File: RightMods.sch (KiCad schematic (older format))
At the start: 9 parts

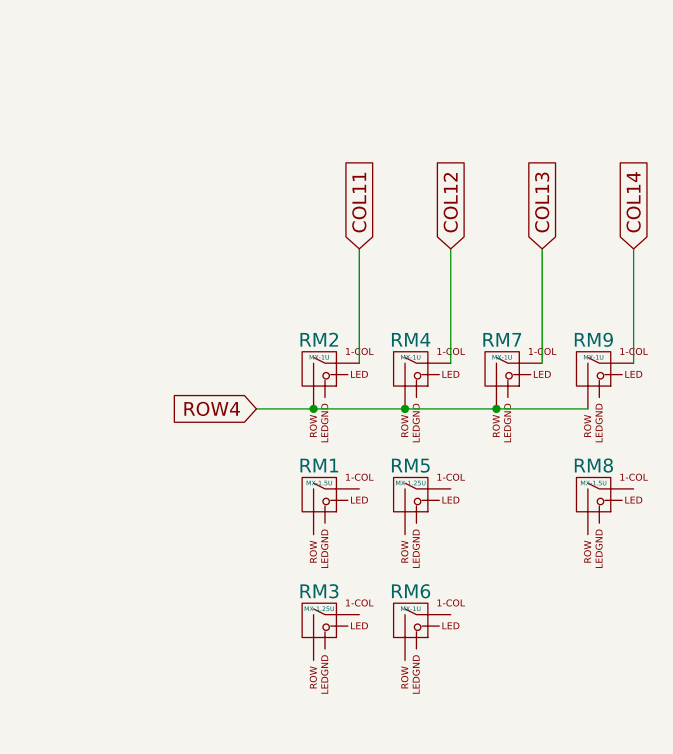
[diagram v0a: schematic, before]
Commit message: Add LEDs
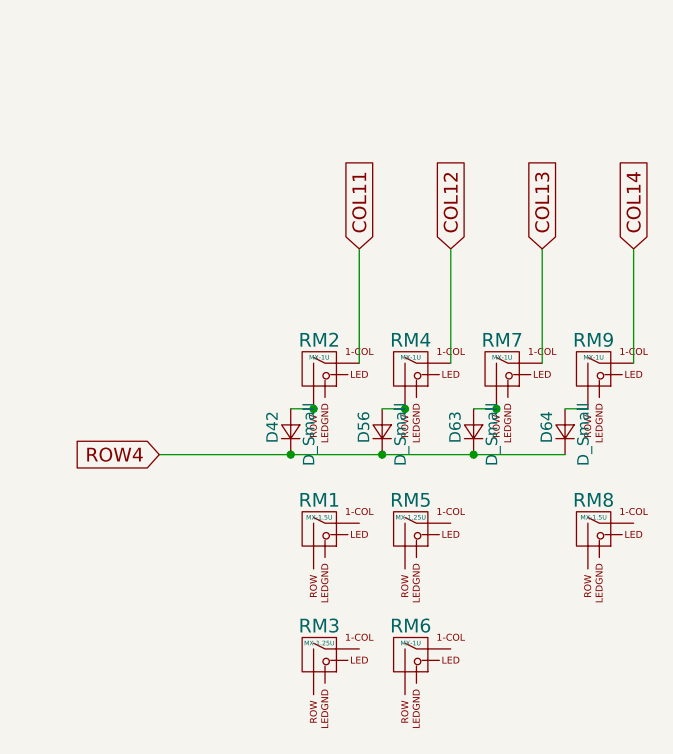
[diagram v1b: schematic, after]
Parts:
- added D42, D56, D63, D64: D_Small, symbol D_Small
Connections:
- net ROW4: now also D42.1 (K), D56.1 (K), D63.1 (K), D64.1 (K); no longer RM2.2 (ROW), RM4.2 (ROW), RM7.2 (ROW), RM9.2 (ROW)
- new net: D42.2 (A), RM2.2 (ROW)
- new net: D56.2 (A), RM4.2 (ROW)
- new net: D63.2 (A), RM7.2 (ROW)
- new net: D64.2 (A), RM9.2 (ROW)
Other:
- moved on the sheet: RM1, RM3, RM5, RM6, RM8
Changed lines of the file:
@@
 L MX-1U RM1
 U 1 1 5A785255
-P 2450 2850
-F 0 "RM1" H 2450 2975 60  0000 C CNN
-F 1 "MX-1.5U" H 2450 2900 20  0000 C CNN
-F 2 "MX_Alps_Hybrid:MX-1.5U-NoLED" H 2425 2825 60  0001 C CNN
-F 3 "" H 2425 2825 60  0001 C CNN
-	1    2450 2850
+P 2450 3000
+F 0 "RM1" H 2450 3125 60  0000 C CNN
+F 1 "MX-1.5U" H 2450 3050 20  0000 C CNN
+F 2 "MX_Alps_Hybrid:MX-1.5U-NoLED" H 2425 2975 60  0001 C CNN
+F 3 "" H 2425 2975 60  0001 C CNN
+	1    2450 3000
 	1    0    0    -1
 $EndComp
@@
 L MX-1U RM3
 U 1 1 5A785291
-P 2450 3400
-F 0 "RM3" H 2450 3525 60  0000 C CNN
-F 1 "MX-1.25U" H 2450 3450 20  0000 C CNN
-F 2 "MX_Alps_Hybrid:MX-1.25U-NoLED" H 2425 3375 60  0001 C CNN
-F 3 "" H 2425 3375 60  0001 C CNN
-	1    2450 3400
+P 2450 3550
+F 0 "RM3" H 2450 3675 60  0000 C CNN
+F 1 "MX-1.25U" H 2450 3600 20  0000 C CNN
+F 2 "MX_Alps_Hybrid:MX-1.25U-NoLED" H 2425 3525 60  0001 C CNN
+F 3 "" H 2425 3525 60  0001 C CNN
+	1    2450 3550
 	1    0    0    -1
 $EndComp
@@
 L MX-1U RM5
 U 1 1 5A785372
-P 2850 2850
-F 0 "RM5" H 2850 2975 60  0000 C CNN
-F 1 "MX-1.25U" H 2850 2900 20  0000 C CNN
-F 2 "MX_Alps_Hybrid:MX-1.25U-NoLED" H 2825 2825 60  0001 C CNN
-F 3 "" H 2825 2825 60  0001 C CNN
-	1    2850 2850
+P 2850 3000
+F 0 "RM5" H 2850 3125 60  0000 C CNN
+F 1 "MX-1.25U" H 2850 3050 20  0000 C CNN
+F 2 "MX_Alps_Hybrid:MX-1.25U-NoLED" H 2825 2975 60  0001 C CNN
+F 3 "" H 2825 2975 60  0001 C CNN
+	1    2850 3000
 	1    0    0    -1
 $EndComp
@@
 L MX-1U RM6
 U 1 1 5A7856EF
-P 2850 3400
-F 0 "RM6" H 2850 3525 60  0000 C CNN
-F 1 "MX-1U" H 2850 3450 20  0000 C CNN
-F 2 "MX_Alps_Hybrid:MX-1U-NoLED" H 2825 3375 60  0001 C CNN
-F 3 "" H 2825 3375 60  0001 C CNN
-	1    2850 3400
+P 2850 3550
+F 0 "RM6" H 2850 3675 60  0000 C CNN
+F 1 "MX-1U" H 2850 3600 20  0000 C CNN
+F 2 "MX_Alps_Hybrid:MX-1U-NoLED" H 2825 3525 60  0001 C CNN
+F 3 "" H 2825 3525 60  0001 C CNN
+	1    2850 3550
 	1    0    0    -1
 $EndComp
@@
 L MX-1U RM8
 U 1 1 5A7858EC
-P 3650 2850
-F 0 "RM8" H 3650 2975 60  0000 C CNN
-F 1 "MX-1.5U" H 3650 2900 20  0000 C CNN
-F 2 "MX_Alps_Hybrid:MX-1.5U-NoLED" H 3625 2825 60  0001 C CNN
-F 3 "" H 3625 2825 60  0001 C CNN
-	1    3650 2850
+P 3650 3000
+F 0 "RM8" H 3650 3125 60  0000 C CNN
+F 1 "MX-1.5U" H 3650 3050 20  0000 C CNN
+F 2 "MX_Alps_Hybrid:MX-1.5U-NoLED" H 3625 2975 60  0001 C CNN
+F 3 "" H 3625 2975 60  0001 C CNN
+	1    3650 3000
 	1    0    0    -1
 $EndComp
@@
 Text GLabel 3825 1775 1    60   Input ~ 0
 COL14
-Wire Wire Line
-	2175 2475 3625 2475
 Connection ~ 3225 2475
 Connection ~ 2825 2475
 Connection ~ 2425 2475
-Text GLabel 2175 2475 0    60   Input ~ 0
+Text GLabel 1750 2675 0    60   Input ~ 0
 ROW4
+$Comp
+L D_Small D42
+U 1 1 5A789BFF
+P 2325 2575
+F 0 "D42" H 2275 2655 50  0000 L CNN
+F 1 "D_Small" H 2175 2495 50  0000 L CNN
+F 2 "" V 2325 2575 50  0001 C CNN
+F 3 "" V 2325 2575 50  0001 C CNN
+	1    2325 2575
+	0    -1   -1   0
+$EndComp
+$Comp
+L D_Small D56
+U 1 1 5A789E12
+P 2725 2575
+F 0 "D56" H 2675 2655 50  0000 L CNN
+F 1 "D_Small" H 2575 2495 50  0000 L CNN
+F 2 "" V 2725 2575 50  0001 C CNN
+F 3 "" V 2725 2575 50  0001 C CNN
+	1    2725 2575
+	0    -1   -1   0
+$EndComp
+$Comp
+L D_Small D63
+U 1 1 5A789F57
+P 3125 2575
+F 0 "D63" H 3075 2655 50  0000 L CNN
+F 1 "D_Small" H 2975 2495 50  0000 L CNN
+F 2 "" V 3125 2575 50  0001 C CNN
+F 3 "" V 3125 2575 50  0001 C CNN
+	1    3125 2575
+	0    -1   -1   0
+$EndComp
+$Comp
+L D_Small D64
+U 1 1 5A78A02B
+P 3525 2575
+F 0 "D64" H 3475 2655 50  0000 L CNN
+F 1 "D_Small" H 3375 2495 50  0000 L CNN
+F 2 "" V 3525 2575 50  0001 C CNN
+F 3 "" V 3525 2575 50  0001 C CNN
+	1    3525 2575
+	0    -1   -1   0
+$EndComp
+Wire Wire Line
+	3625 2475 3525 2475
+Wire Wire Line
+	3225 2475 3125 2475
+Wire Wire Line
+	2825 2475 2725 2475
+Wire Wire Line
+	2325 2475 2425 2475
+Wire Wire Line
+	1750 2675 3525 2675
+Connection ~ 3125 2675
+Connection ~ 2725 2675
+Connection ~ 2325 2675
 $EndSCHEMATC

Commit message: Place LEDs and move out diodes
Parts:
- D42, D56, D63, D64: footprint (none) -> Diodes_SMD:D_SOD-123
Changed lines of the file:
@@
 F 0 "D42" H 2275 2655 50  0000 L CNN
 F 1 "D_Small" H 2175 2495 50  0000 L CNN
-F 2 "" V 2325 2575 50  0001 C CNN
+F 2 "Diodes_SMD:D_SOD-123" V 2325 2575 50  0001 C CNN
 F 3 "" V 2325 2575 50  0001 C CNN
 	1    2325 2575
@@
 F 0 "D56" H 2675 2655 50  0000 L CNN
 F 1 "D_Small" H 2575 2495 50  0000 L CNN
-F 2 "" V 2725 2575 50  0001 C CNN
+F 2 "Diodes_SMD:D_SOD-123" V 2725 2575 50  0001 C CNN
 F 3 "" V 2725 2575 50  0001 C CNN
 	1    2725 2575
@@
 F 0 "D63" H 3075 2655 50  0000 L CNN
 F 1 "D_Small" H 2975 2495 50  0000 L CNN
-F 2 "" V 3125 2575 50  0001 C CNN
+F 2 "Diodes_SMD:D_SOD-123" V 3125 2575 50  0001 C CNN
 F 3 "" V 3125 2575 50  0001 C CNN
 	1    3125 2575
@@
 F 0 "D64" H 3475 2655 50  0000 L CNN
 F 1 "D_Small" H 3375 2495 50  0000 L CNN
-F 2 "" V 3525 2575 50  0001 C CNN
+F 2 "Diodes_SMD:D_SOD-123" V 3525 2575 50  0001 C CNN
 F 3 "" V 3525 2575 50  0001 C CNN
 	1    3525 2575

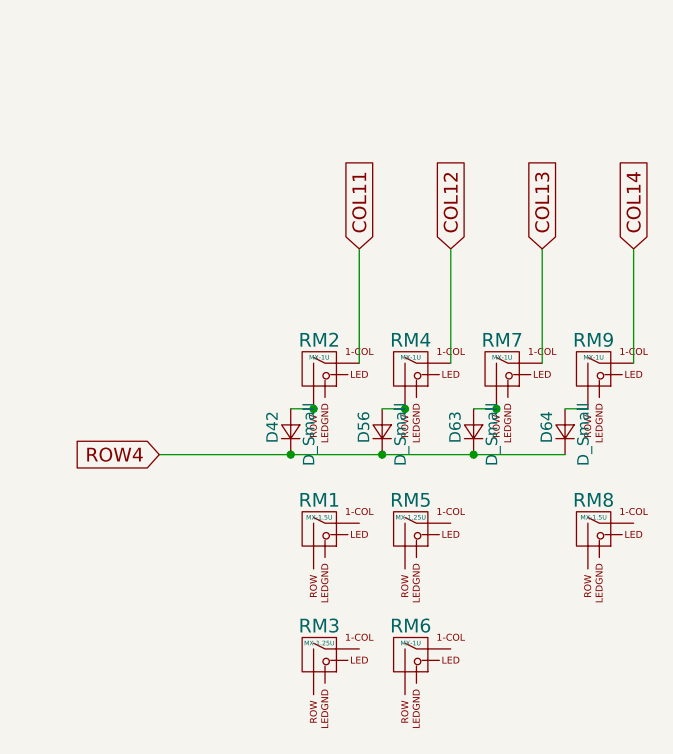
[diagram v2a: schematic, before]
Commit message: Route RM1, right mod leds
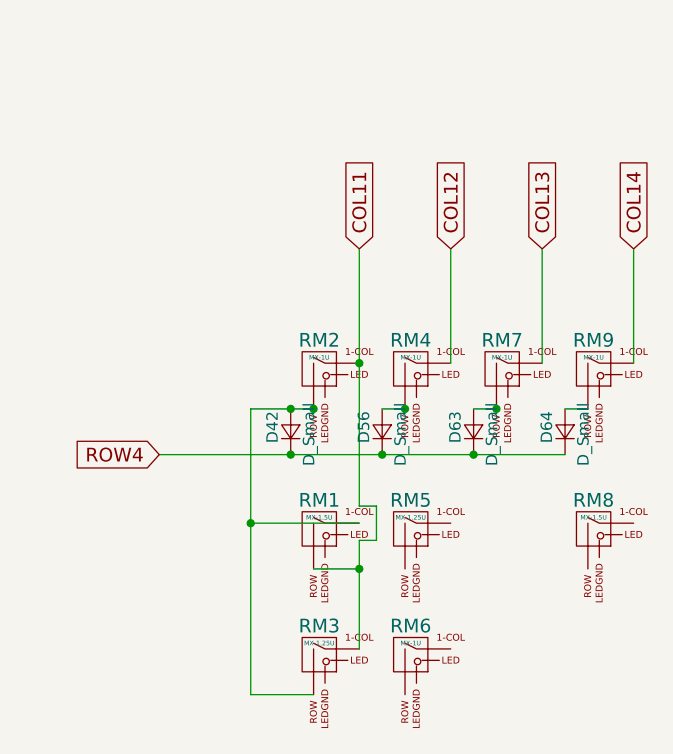
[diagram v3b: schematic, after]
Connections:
- net COL11: now also RM1.2 (ROW), RM3.1 (COL)
- net at D42.2 (A), RM2.2 (ROW): now also RM1.1 (COL), RM3.2 (ROW)
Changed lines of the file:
@@
 $EndComp
 Wire Wire Line
-	2625 2275 2625 1775
+	2625 1775 2625 2900
 Text GLabel 2625 1775 1    60   Input ~ 0
 COL11
@@
 	2825 2475 2725 2475
 Wire Wire Line
-	2325 2475 2425 2475
+	2150 2475 2425 2475
 Wire Wire Line
 	1750 2675 3525 2675
@@
 Connection ~ 2725 2675
 Connection ~ 2325 2675
+Wire Wire Line
+	2625 2900 2700 2900
+Wire Wire Line
+	2700 2900 2700 3050
+Wire Wire Line
+	2700 3050 2625 3050
+Wire Wire Line
+	2625 3050 2625 3525
+Connection ~ 2625 2275
+Wire Wire Line
+	2150 2475 2150 3725
+Wire Wire Line
+	2150 3725 2425 3725
+Connection ~ 2325 2475
+Wire Wire Line
+	2625 2975 2150 2975
+Connection ~ 2150 2975
+Wire Wire Line
+	2425 3175 2625 3175
+Connection ~ 2625 3175
 $EndSCHEMATC

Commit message: Finish routing
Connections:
- net COL12: now also RM5.2 (ROW), RM6.2 (ROW)
- net COL14: now also RM8.1 (COL), RM9.2 (ROW); no longer RM9.1 (COL)
- net at D56.2 (A), RM4.2 (ROW): now also RM5.1 (COL), RM6.1 (COL)
- net at D64.2 (A): now also RM8.2 (ROW), RM9.1 (COL); no longer RM9.2 (ROW)
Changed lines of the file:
@@
 	1    0    0    -1
 $EndComp
-Wire Wire Line
-	2625 1775 2625 2900
 Text GLabel 2625 1775 1    60   Input ~ 0
 COL11
-Wire Wire Line
-	3025 2275 3025 1775
 Text GLabel 3025 1775 1    60   Input ~ 0
 COL12
-Wire Wire Line
-	3425 2275 3425 1775
 Text GLabel 3425 1775 1    60   Input ~ 0
 COL13
-Wire Wire Line
-	3825 2275 3825 1775
 Text GLabel 3825 1775 1    60   Input ~ 0
 COL14
-Connection ~ 3225 2475
-Connection ~ 2825 2475
-Connection ~ 2425 2475
 Text GLabel 1750 2675 0    60   Input ~ 0
 ROW4
@@
 $EndComp
 Wire Wire Line
-	3625 2475 3525 2475
+	2625 1775 2625 2900
+Wire Wire Line
+	3025 1775 3025 2800
+Wire Wire Line
+	3425 2275 3425 1775
+Connection ~ 3225 2475
+Connection ~ 2825 2475
+Connection ~ 2425 2475
 Wire Wire Line
 	3225 2475 3125 2475
 Wire Wire Line
-	2825 2475 2725 2475
+	2725 2475 3075 2475
 Wire Wire Line
 	2150 2475 2425 2475
@@
 	2425 3175 2625 3175
 Connection ~ 2625 3175
+Wire Wire Line
+	3025 2800 2750 2800
+Wire Wire Line
+	2750 2800 2750 3725
+Wire Wire Line
+	2750 3175 2825 3175
+Connection ~ 3025 2275
+Wire Wire Line
+	2750 3725 2825 3725
+Connection ~ 2750 3175
+Wire Wire Line
+	3075 2475 3075 3525
+Wire Wire Line
+	3075 2975 3025 2975
+Wire Wire Line
+	3075 3525 3025 3525
+Connection ~ 3075 2975
+Wire Wire Line
+	3525 2475 3525 2275
+Wire Wire Line
+	3525 2275 3825 2275
+Wire Wire Line
+	3825 1775 3825 2200
+Wire Wire Line
+	3825 2200 3900 2200
+Wire Wire Line
+	3900 2200 3900 2975
+Wire Wire Line
+	3900 2475 3625 2475
+Wire Wire Line
+	3900 2975 3825 2975
+Connection ~ 3900 2475
+Wire Wire Line
+	3525 2475 3575 2475
+Wire Wire Line
+	3575 2475 3575 3175
+Wire Wire Line
+	3575 3175 3625 3175
 $EndSCHEMATC

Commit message: Revert LED structure
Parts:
- RM1, RM8: footprint MX_Alps_Hybrid:MX-1.5U-NoLED -> MX_Alps_Hybrid:MX-1.5U
- RM2, RM4, RM6, RM7, RM9: footprint MX_Alps_Hybrid:MX-1U-NoLED -> MX_Alps_Hybrid:MX-1U
- RM3, RM5: footprint MX_Alps_Hybrid:MX-1.25U-NoLED -> MX_Alps_Hybrid:MX-1.25U
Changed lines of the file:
@@
 F 0 "RM2" H 2450 2425 60  0000 C CNN
 F 1 "MX-1U" H 2450 2350 20  0000 C CNN
-F 2 "MX_Alps_Hybrid:MX-1U-NoLED" H 2425 2275 60  0001 C CNN
+F 2 "MX_Alps_Hybrid:MX-1U" H 2425 2275 60  0001 C CNN
 F 3 "" H 2425 2275 60  0001 C CNN
 	1    2450 2300
@@
 F 0 "RM1" H 2450 3125 60  0000 C CNN
 F 1 "MX-1.5U" H 2450 3050 20  0000 C CNN
-F 2 "MX_Alps_Hybrid:MX-1.5U-NoLED" H 2425 2975 60  0001 C CNN
+F 2 "MX_Alps_Hybrid:MX-1.5U" H 2425 2975 60  0001 C CNN
 F 3 "" H 2425 2975 60  0001 C CNN
 	1    2450 3000
@@
 F 0 "RM3" H 2450 3675 60  0000 C CNN
 F 1 "MX-1.25U" H 2450 3600 20  0000 C CNN
-F 2 "MX_Alps_Hybrid:MX-1.25U-NoLED" H 2425 3525 60  0001 C CNN
+F 2 "MX_Alps_Hybrid:MX-1.25U" H 2425 3525 60  0001 C CNN
 F 3 "" H 2425 3525 60  0001 C CNN
 	1    2450 3550
@@
 F 0 "RM4" H 2850 2425 60  0000 C CNN
 F 1 "MX-1U" H 2850 2350 20  0000 C CNN
-F 2 "MX_Alps_Hybrid:MX-1U-NoLED" H 2825 2275 60  0001 C CNN
+F 2 "MX_Alps_Hybrid:MX-1U" H 2825 2275 60  0001 C CNN
 F 3 "" H 2825 2275 60  0001 C CNN
 	1    2850 2300
@@
 F 0 "RM5" H 2850 3125 60  0000 C CNN
 F 1 "MX-1.25U" H 2850 3050 20  0000 C CNN
-F 2 "MX_Alps_Hybrid:MX-1.25U-NoLED" H 2825 2975 60  0001 C CNN
+F 2 "MX_Alps_Hybrid:MX-1.25U" H 2825 2975 60  0001 C CNN
 F 3 "" H 2825 2975 60  0001 C CNN
 	1    2850 3000
@@
 F 0 "RM7" H 3250 2425 60  0000 C CNN
 F 1 "MX-1U" H 3250 2350 20  0000 C CNN
-F 2 "MX_Alps_Hybrid:MX-1U-NoLED" H 3225 2275 60  0001 C CNN
+F 2 "MX_Alps_Hybrid:MX-1U" H 3225 2275 60  0001 C CNN
 F 3 "" H 3225 2275 60  0001 C CNN
 	1    3250 2300
@@
 F 0 "RM9" H 3650 2425 60  0000 C CNN
 F 1 "MX-1U" H 3650 2350 20  0000 C CNN
-F 2 "MX_Alps_Hybrid:MX-1U-NoLED" H 3625 2275 60  0001 C CNN
+F 2 "MX_Alps_Hybrid:MX-1U" H 3625 2275 60  0001 C CNN
 F 3 "" H 3625 2275 60  0001 C CNN
 	1    3650 2300
@@
 F 0 "RM6" H 2850 3675 60  0000 C CNN
 F 1 "MX-1U" H 2850 3600 20  0000 C CNN
-F 2 "MX_Alps_Hybrid:MX-1U-NoLED" H 2825 3525 60  0001 C CNN
+F 2 "MX_Alps_Hybrid:MX-1U" H 2825 3525 60  0001 C CNN
 F 3 "" H 2825 3525 60  0001 C CNN
 	1    2850 3550
@@
 F 0 "RM8" H 3650 3125 60  0000 C CNN
 F 1 "MX-1.5U" H 3650 3050 20  0000 C CNN
-F 2 "MX_Alps_Hybrid:MX-1.5U-NoLED" H 3625 2975 60  0001 C CNN
+F 2 "MX_Alps_Hybrid:MX-1.5U" H 3625 2975 60  0001 C CNN
 F 3 "" H 3625 2975 60  0001 C CNN
 	1    3650 3000

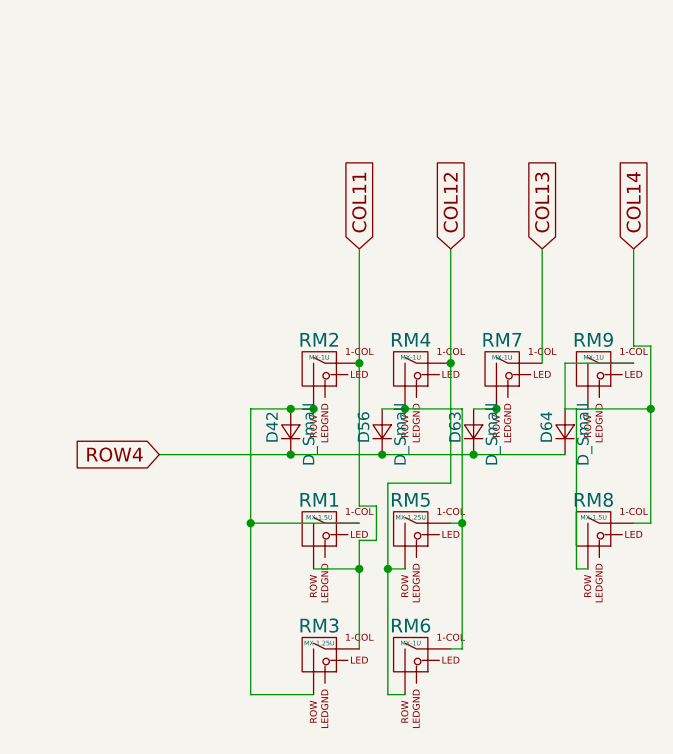
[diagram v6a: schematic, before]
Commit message: Wire LED rows
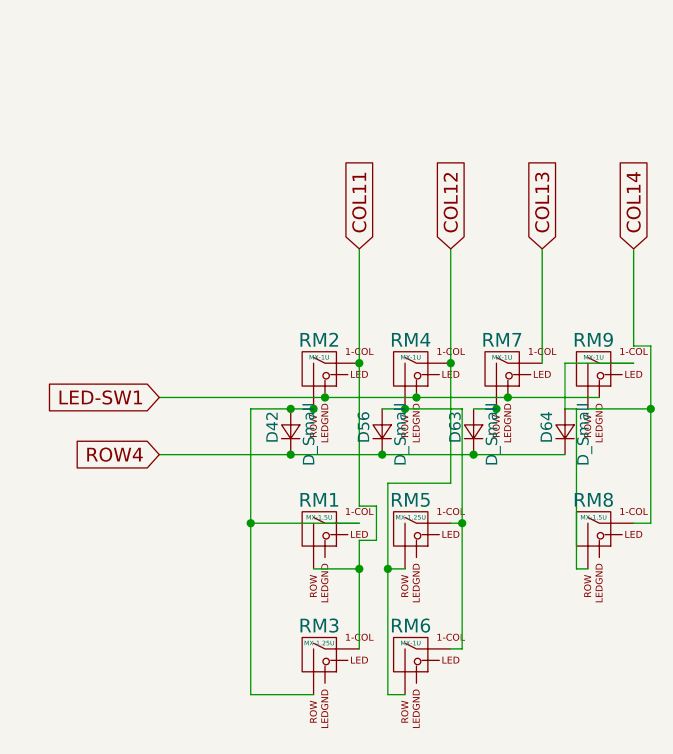
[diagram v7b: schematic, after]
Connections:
- net LED-SW1: now reaches RM2.4 (LEDGND)
- net LED-SW1: now also RM4.4 (LEDGND), RM7.4 (LEDGND), RM9.4 (LEDGND)
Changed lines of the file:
@@
 Wire Wire Line
 	3575 3175 3625 3175
+Wire Wire Line
+	1750 2425 3675 2425
+Connection ~ 3275 2425
+Connection ~ 2875 2425
+Connection ~ 2475 2425
+Text GLabel 1750 2425 0    60   Input ~ 0
+LED-SW1
 $EndSCHEMATC

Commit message: Begin routing
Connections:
- net LED-CS12: now reaches RM2.3 (LED)
- net LED-CS13: now reaches RM4.3 (LED)
- net LED-CS14: now reaches RM7.3 (LED)
- net LED-CS15: now reaches RM9.3 (LED)
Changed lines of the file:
@@
 Text GLabel 1750 2425 0    60   Input ~ 0
 LED-SW1
+Wire Wire Line
+	3775 2325 3775 1425
+Text GLabel 3775 1425 1    60   Input ~ 0
+LED-CS15
+Wire Wire Line
+	3375 2325 3375 1425
+Text GLabel 3375 1425 1    60   Input ~ 0
+LED-CS14
+Wire Wire Line
+	2975 2325 2975 1425
+Text GLabel 2975 1425 1    60   Input ~ 0
+LED-CS13
+Wire Wire Line
+	2575 2325 2575 1425
+Text GLabel 2575 1425 1    60   Input ~ 0
+LED-CS12
 $EndSCHEMATC
